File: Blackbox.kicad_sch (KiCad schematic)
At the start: 40 parts, among them CN1 SM04B-SRSS-TB (LF)(SN), U1 SN65HVD232DR, U2 STM32G0B1CCT6, U3 BM06B-SRSS-TB(LF)(SN), X2 DSX321G-48M

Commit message: Add PCB schematic PDF
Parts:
- added D17: 0603ESDA-05N, EasyEDA:D0603-BI, symbol EasyEDA:0603ESDA-05N
- added R8: 10kΩ, EasyEDA:R0603, symbol EasyEDA:FRC0603J103TS
- C1, C2: value 0402CG120J500NT: 12pF -> 12pF
- C3, C4, C5, C6, C7, C8: value CC0603KRX7R9BB104 -> 100nF
- R1: value 100kΩ -> 10kΩ
- R2, R3, R4, R5, R6, R7: value FRC0603J103TS -> 10kΩ
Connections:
- net +3V3: now also C8.2, R8.1; no longer C8.1
- net GND: now also C8.1, D17.2; no longer C8.2
- net CD: now reaches U2.14 (PA3)
- net CD: now also Card1.9 (CD), D17.1, R8.2
- no-connect marks 14 -> 48
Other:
- moved on the sheet: D14, D23, D5

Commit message: Update schematic and PCB with latest changes
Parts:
- removed C7: 100nF, EasyEDA:C0603, symbol EasyEDA:CC0603KRX7R9BB104
- removed D14, D15, D21: 0603ESDA-05N, EasyEDA:D0603-BI, symbol EasyEDA:0603ESDA-05N
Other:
- moved on the sheet: D12

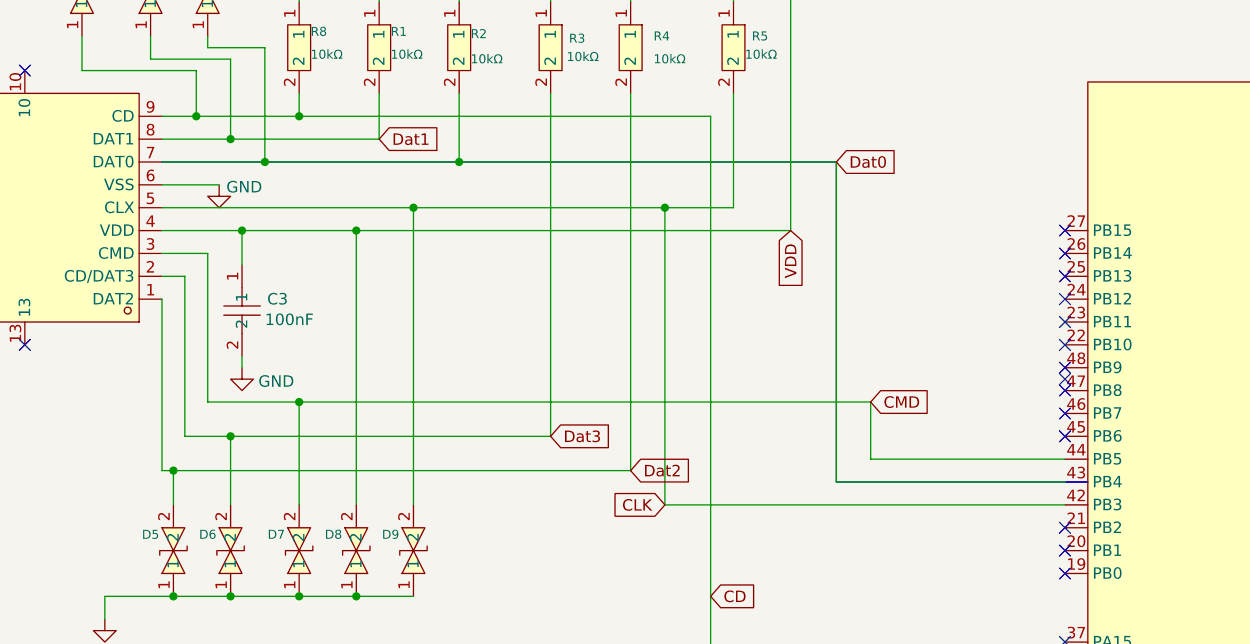
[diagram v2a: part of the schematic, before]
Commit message: The PCB connections are completed
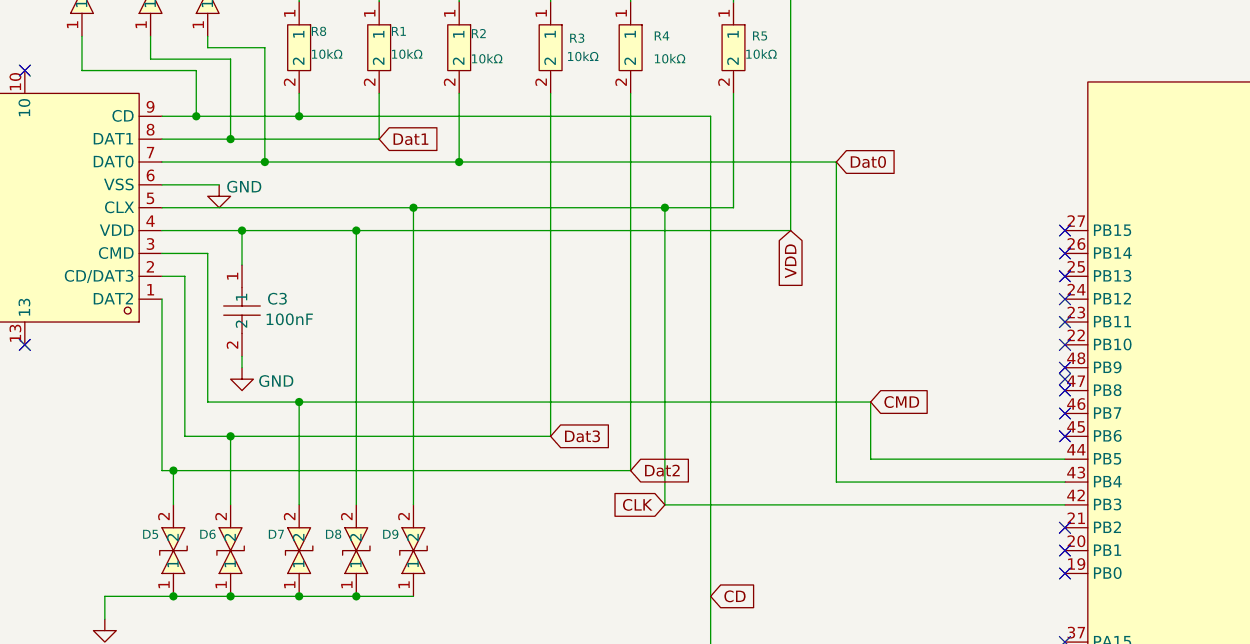
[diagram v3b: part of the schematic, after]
